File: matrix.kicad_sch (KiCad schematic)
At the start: 143 parts

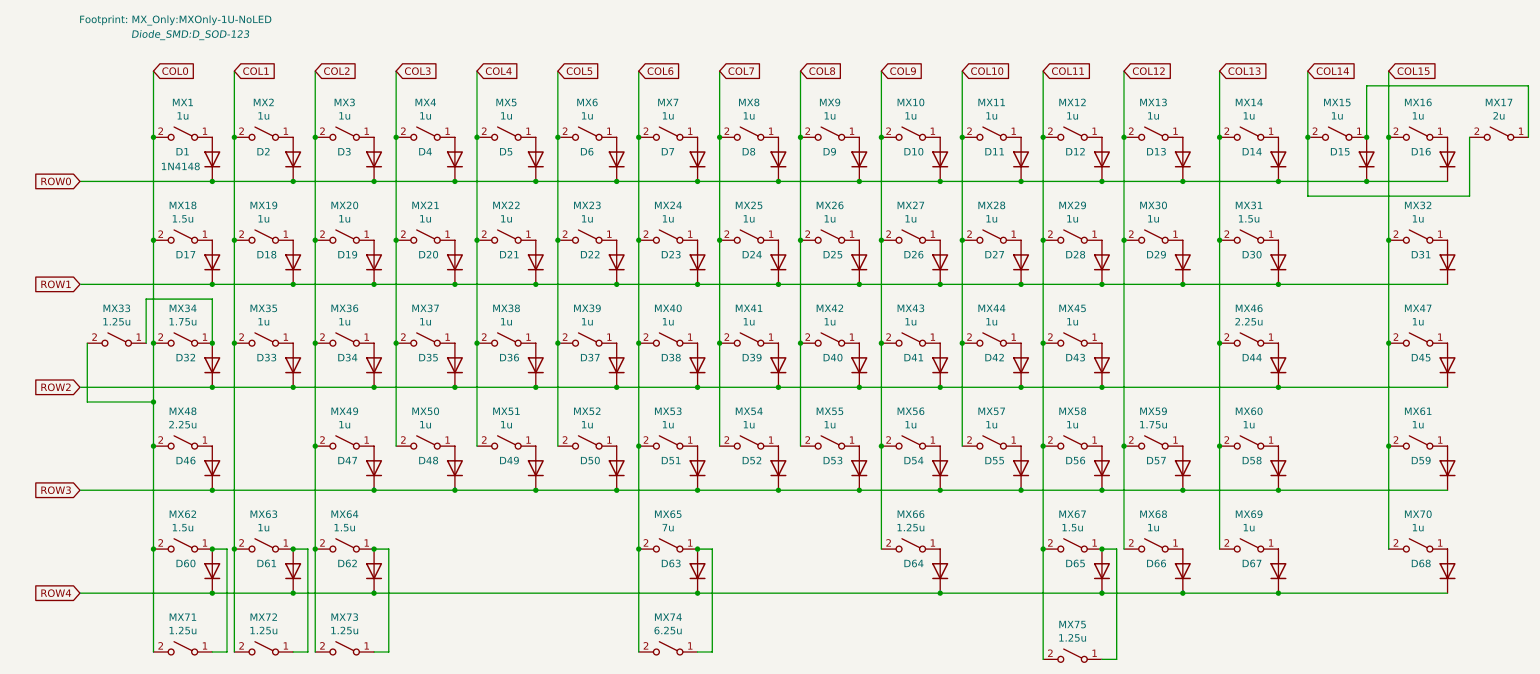
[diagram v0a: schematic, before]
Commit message: Added Hotswap + 2 MCU layouts
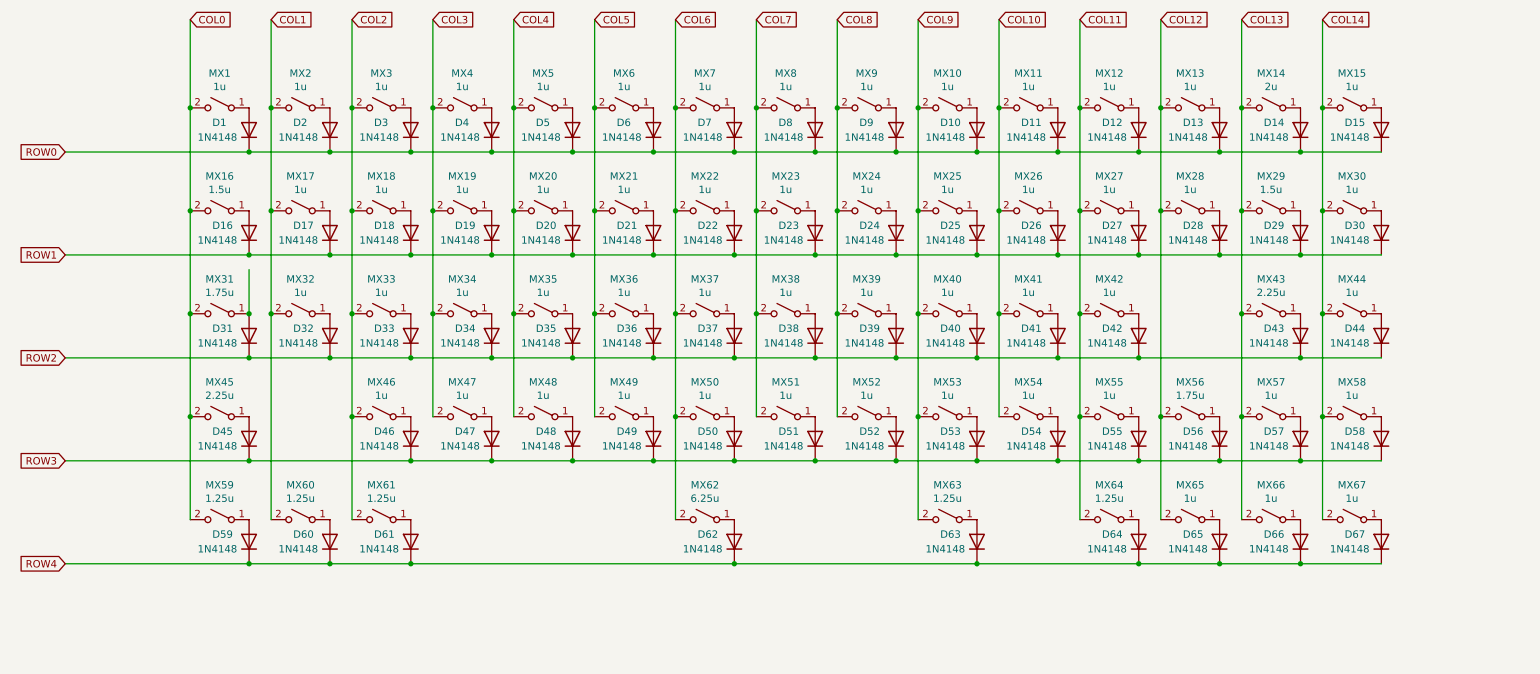
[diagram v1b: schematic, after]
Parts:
- removed D1, D10, D11, D12, D13, D14, D15, D16, D17, D18, D19, D2, D20, D21, D22, D23, D24, D25, D26, D27, D28, D29, D3, D30, D31, D32, D33, D34, D35, D36, D37, D38, D39, D4, D40, D41, D42, D43, D44, D45, D46, D47, D48, D49, D5, D50, D51, D52, D53, D54, D55, D56, D57, D58, D59, D6, D60, D61, D62, D63, D64, D65, D66, D67, D68, D7, D8, D9: 1N4148, Diode_SMD:D_SOD-123, symbol Device:D
- removed MX1, MX10, MX11, MX12, MX13, MX14, MX15, MX16, MX19, MX2, MX20, MX21, MX22, MX23, MX24, MX25, MX26, MX27, MX28, MX29, MX3, MX30, MX32, MX35, MX36, MX37, MX38, MX39, MX4, MX40, MX41, MX42, MX43, MX44, MX45, MX47, MX49, MX5, MX50, MX51, MX52, MX53, MX54, MX55, MX56, MX57, MX58, MX6, MX60, MX61, MX63, MX68, MX69, MX7, MX70, MX8, MX9: 1u, MX_Only:MXOnly-1U-NoLED, symbol Switch:SW_SPST
- removed MX17: 2u, MX_Only:MXOnly-2U-NoLED, symbol Switch:SW_SPST
- removed MX18, MX31, MX62, MX64, MX67: 1.5u, MX_Only:MXOnly-1.5U-NoLED, symbol Switch:SW_SPST
- removed MX33, MX66, MX71, MX72, MX73, MX75: 1.25u, MX_Only:MXOnly-1.25U-NoLED, symbol Switch:SW_SPST
- removed MX34, MX59: 1.75u, MX_Only:MXOnly-1.75U-NoLED, symbol Switch:SW_SPST
- removed MX46, MX48: 2.25u, MX_Only:MXOnly-2.25U-NoLED, symbol Switch:SW_SPST
- removed MX65: 7u, MX_Only:MXOnly-7U-ReversedStabilizers-NoLED, symbol Switch:SW_SPST
- removed MX74: 6.25u, MX_Only:MXOnly-6.25U-ReversedStabilizers-NoLED, symbol Switch:SW_SPST
- added D1, D10, D11, D12, D13, D14, D15, D16, D17, D18, D19, D2, D20, D21, D22, D23, D24, D25, D26, D27, D28, D29, D3, D30, D31, D32, D33, D34, D35, D36, D37, D38, D39, D4, D40, D41, D42, D43, D44, D45, D46, D47, D48, D49, D5, D50, D51, D52, D53, D54, D55, D56, D57, D58, D59, D6, D60, D61, D62, D63, D64, D65, D66, D67, D7, D8, D9: 1N4148, Diode_SMD:D_SOD-123, symbol Diode:1N4148
- added MX1, MX10, MX11, MX12, MX13, MX15, MX17, MX18, MX19, MX2, MX20, MX21, MX22, MX23, MX24, MX25, MX26, MX27, MX28, MX3, MX30, MX32, MX33, MX34, MX35, MX36, MX37, MX38, MX39, MX4, MX40, MX41, MX42, MX44, MX46, MX47, MX48, MX49, MX5, MX50, MX51, MX52, MX53, MX54, MX55, MX57, MX58, MX6, MX65, MX66, MX67, MX7, MX8, MX9: 1u, MX_Only:MXOnly-1U-Hotswap, symbol mikeneko-65-pcb-rescue:SW_SPST-Switch
- added MX14: 2u, MX_Only:MXOnly-2U-Hotswap, symbol mikeneko-65-pcb-rescue:SW_SPST-Switch
- added MX16, MX29: 1.5u, MX_Only:MXOnly-1.5U-Hotswap, symbol mikeneko-65-pcb-rescue:SW_SPST-Switch
- added MX31, MX56: 1.75u, MX_Only:MXOnly-1.75U-Hotswap, symbol mikeneko-65-pcb-rescue:SW_SPST-Switch
- added MX43, MX45: 2.25u, MX_Only:MXOnly-2.25U-Hotswap, symbol mikeneko-65-pcb-rescue:SW_SPST-Switch
- added MX59, MX60, MX61, MX63, MX64: 1.25u, MX_Only:MXOnly-1.25U-Hotswap, symbol mikeneko-65-pcb-rescue:SW_SPST-Switch
- added MX62: 6.25u, MX_Only:MXOnly-6.25U-Hotswap-ReversedStabilizers, symbol mikeneko-65-pcb-rescue:SW_SPST-Switch
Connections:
- net COL0: now also MX1.2 (B), MX16.2 (B), MX31.2 (B), MX45.2 (B), MX59.2 (B)
- net COL1: now also MX17.2 (B), MX2.2 (B), MX32.2 (B), MX60.2 (B)
- net COL10: now also MX11.2 (B), MX26.2 (B), MX41.2 (B), MX54.2 (B)
- net COL11: now also MX12.2 (B), MX27.2 (B), MX42.2 (B), MX55.2 (B), MX64.2 (B)
- net COL12: now also MX13.2 (B), MX28.2 (B), MX56.2 (B), MX65.2 (B)
- net COL13: now also MX14.2 (B), MX29.2 (B), MX43.2 (B), MX57.2 (B), MX66.2 (B)
- net COL14: now also MX15.2 (B), MX30.2 (B), MX44.2 (B), MX58.2 (B), MX67.2 (B)
- net COL2: now also MX18.2 (B), MX3.2 (B), MX33.2 (B), MX46.2 (B), MX61.2 (B)
- net COL3: now also MX19.2 (B), MX34.2 (B), MX4.2 (B), MX47.2 (B)
- net COL4: now also MX20.2 (B), MX35.2 (B), MX48.2 (B), MX5.2 (B)
- net COL5: now also MX21.2 (B), MX36.2 (B), MX49.2 (B), MX6.2 (B)
- net COL6: now also MX22.2 (B), MX37.2 (B), MX50.2 (B), MX62.2 (B), MX7.2 (B)
- net COL7: now also MX23.2 (B), MX38.2 (B), MX51.2 (B), MX8.2 (B)
- net COL8: now also MX24.2 (B), MX39.2 (B), MX52.2 (B), MX9.2 (B)
- net COL9: now also MX10.2 (B), MX25.2 (B), MX40.2 (B), MX53.2 (B), MX63.2 (B)
- net ROW0: now also D1.1 (K), D10.1 (K), D11.1 (K), D12.1 (K), D13.1 (K), D14.1 (K), D15.1 (K), D2.1 (K), D3.1 (K), D4.1 (K), D5.1 (K), D6.1 (K), D7.1 (K), D8.1 (K), D9.1 (K)
- net ROW1: now also D16.1 (K), D17.1 (K), D18.1 (K), D19.1 (K), D20.1 (K), D21.1 (K), D22.1 (K), D23.1 (K), D24.1 (K), D25.1 (K), D26.1 (K), D27.1 (K), D28.1 (K), D29.1 (K), D30.1 (K)
- net ROW2: now also D31.1 (K), D32.1 (K), D33.1 (K), D34.1 (K), D35.1 (K), D36.1 (K), D37.1 (K), D38.1 (K), D39.1 (K), D40.1 (K), D41.1 (K), D42.1 (K), D43.1 (K), D44.1 (K)
- net ROW3: now also D45.1 (K), D46.1 (K), D47.1 (K), D48.1 (K), D49.1 (K), D50.1 (K), D51.1 (K), D52.1 (K), D53.1 (K), D54.1 (K), D55.1 (K), D56.1 (K), D57.1 (K), D58.1 (K)
- net ROW4: now also D59.1 (K), D60.1 (K), D61.1 (K), D62.1 (K), D63.1 (K), D64.1 (K), D65.1 (K), D66.1 (K), D67.1 (K)
- new net: D56.2 (A), MX56.1 (A)
- new net: D54.2 (A), MX54.1 (A)
- new net: D26.2 (A), MX26.1 (A)
- new net: D20.2 (A), MX20.1 (A)
- new net: D40.2 (A), MX40.1 (A)
- new net: D61.2 (A), MX61.1 (A)
- new net: D59.2 (A), MX59.1 (A)
- new net: D67.2 (A), MX67.1 (A)
- new net: D14.2 (A), MX14.1 (A)
- new net: D58.2 (A), MX58.1 (A)
- new net: D66.2 (A), MX66.1 (A)
- new net: D9.2 (A), MX9.1 (A)
- new net: D5.2 (A), MX5.1 (A)
- new net: D55.2 (A), MX55.1 (A)
- new net: D41.2 (A), MX41.1 (A)
- new net: D30.2 (A), MX30.1 (A)
- new net: D22.2 (A), MX22.1 (A)
- new net: D15.2 (A), MX15.1 (A)
- new net: D8.2 (A), MX8.1 (A)
- new net: D35.2 (A), MX35.1 (A)
- new net: D32.2 (A), MX32.1 (A)
- new net: D7.2 (A), MX7.1 (A)
- new net: D12.2 (A), MX12.1 (A)
- new net: D1.2 (A), MX1.1 (A)
- new net: D33.2 (A), MX33.1 (A)
- new net: D4.2 (A), MX4.1 (A)
- new net: D60.2 (A), MX60.1 (A)
- new net: D52.2 (A), MX52.1 (A)
- new net: D24.2 (A), MX24.1 (A)
- new net: D29.2 (A), MX29.1 (A)
- new net: D10.2 (A), MX10.1 (A)
- new net: D11.2 (A), MX11.1 (A)
- new net: D6.2 (A), MX6.1 (A)
- new net: D3.2 (A), MX3.1 (A)
- new net: D42.2 (A), MX42.1 (A)
- new net: D38.2 (A), MX38.1 (A)
- new net: D47.2 (A), MX47.1 (A)
- new net: D21.2 (A), MX21.1 (A)
- new net: D18.2 (A), MX18.1 (A)
- new net: D53.2 (A), MX53.1 (A)
- new net: D25.2 (A), MX25.1 (A)
- new net: D57.2 (A), MX57.1 (A)
- new net: D49.2 (A), MX49.1 (A)
- new net: D45.2 (A), MX45.1 (A)
- new net: D64.2 (A), MX64.1 (A)
- new net: D63.2 (A), MX63.1 (A)
- new net: D50.2 (A), MX50.1 (A)
- new net: D16.2 (A), MX16.1 (A)
- new net: D51.2 (A), MX51.1 (A)
- new net: D27.2 (A), MX27.1 (A)
- new net: D43.2 (A), MX43.1 (A)
- new net: D39.2 (A), MX39.1 (A)
- new net: D17.2 (A), MX17.1 (A)
- new net: D13.2 (A), MX13.1 (A)
- new net: D31.2 (A), MX31.1 (A)
- new net: D44.2 (A), MX44.1 (A)
- new net: D36.2 (A), MX36.1 (A)
- new net: D28.2 (A), MX28.1 (A)
- new net: D19.2 (A), MX19.1 (A)
- new net: D46.2 (A), MX46.1 (A)
- new net: D62.2 (A), MX62.1 (A)
- new net: D2.2 (A), MX2.1 (A)
- new net: D48.2 (A), MX48.1 (A)
- new net: D37.2 (A), MX37.1 (A)
- new net: D34.2 (A), MX34.1 (A)
- new net: D65.2 (A), MX65.1 (A)
- new net: D23.2 (A), MX23.1 (A)
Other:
- title: Jaws65 -> (none)
